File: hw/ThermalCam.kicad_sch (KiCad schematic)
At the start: 48 parts, among them J1 Conn_02x20_Counter_Clockwise, J2 Conn_01x04, J3 Conn_01x06, U1 GW1NR-9_QN882, X1 ASE-25MHz

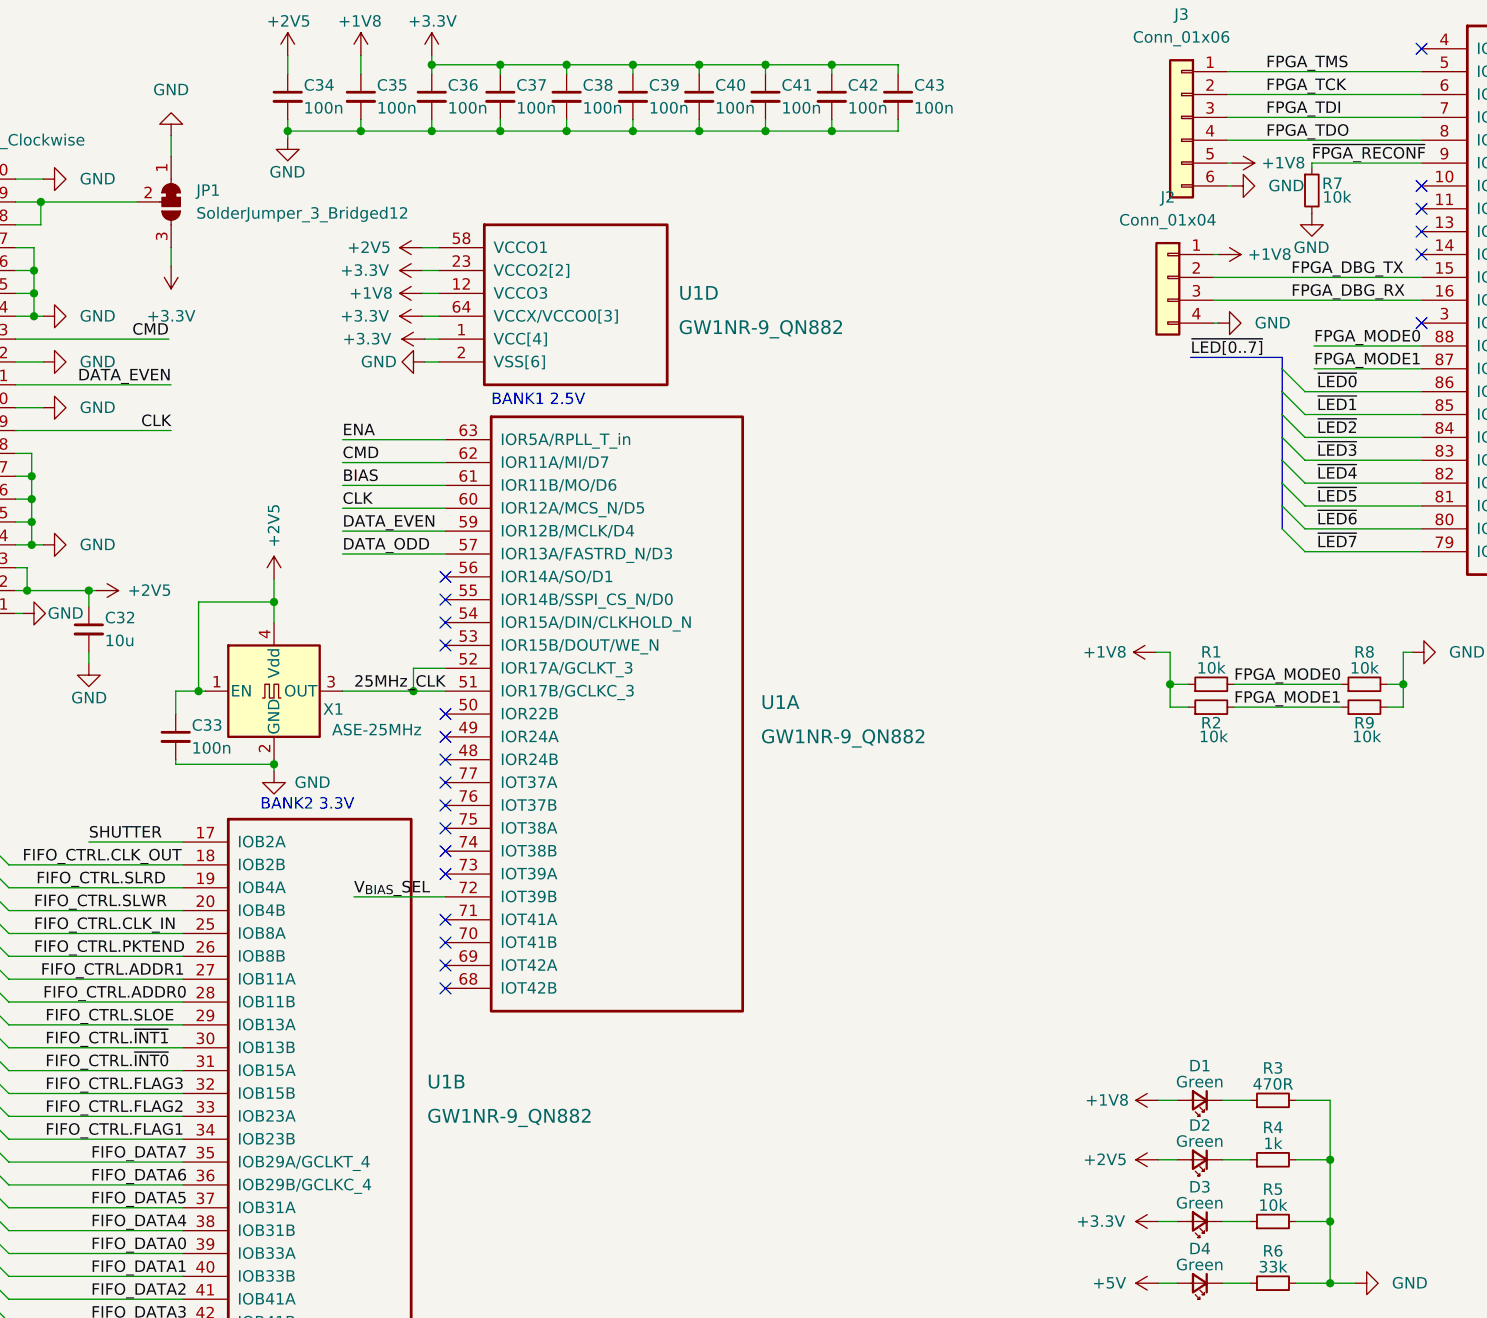
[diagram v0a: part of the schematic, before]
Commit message: schematic fixes and adding sw section
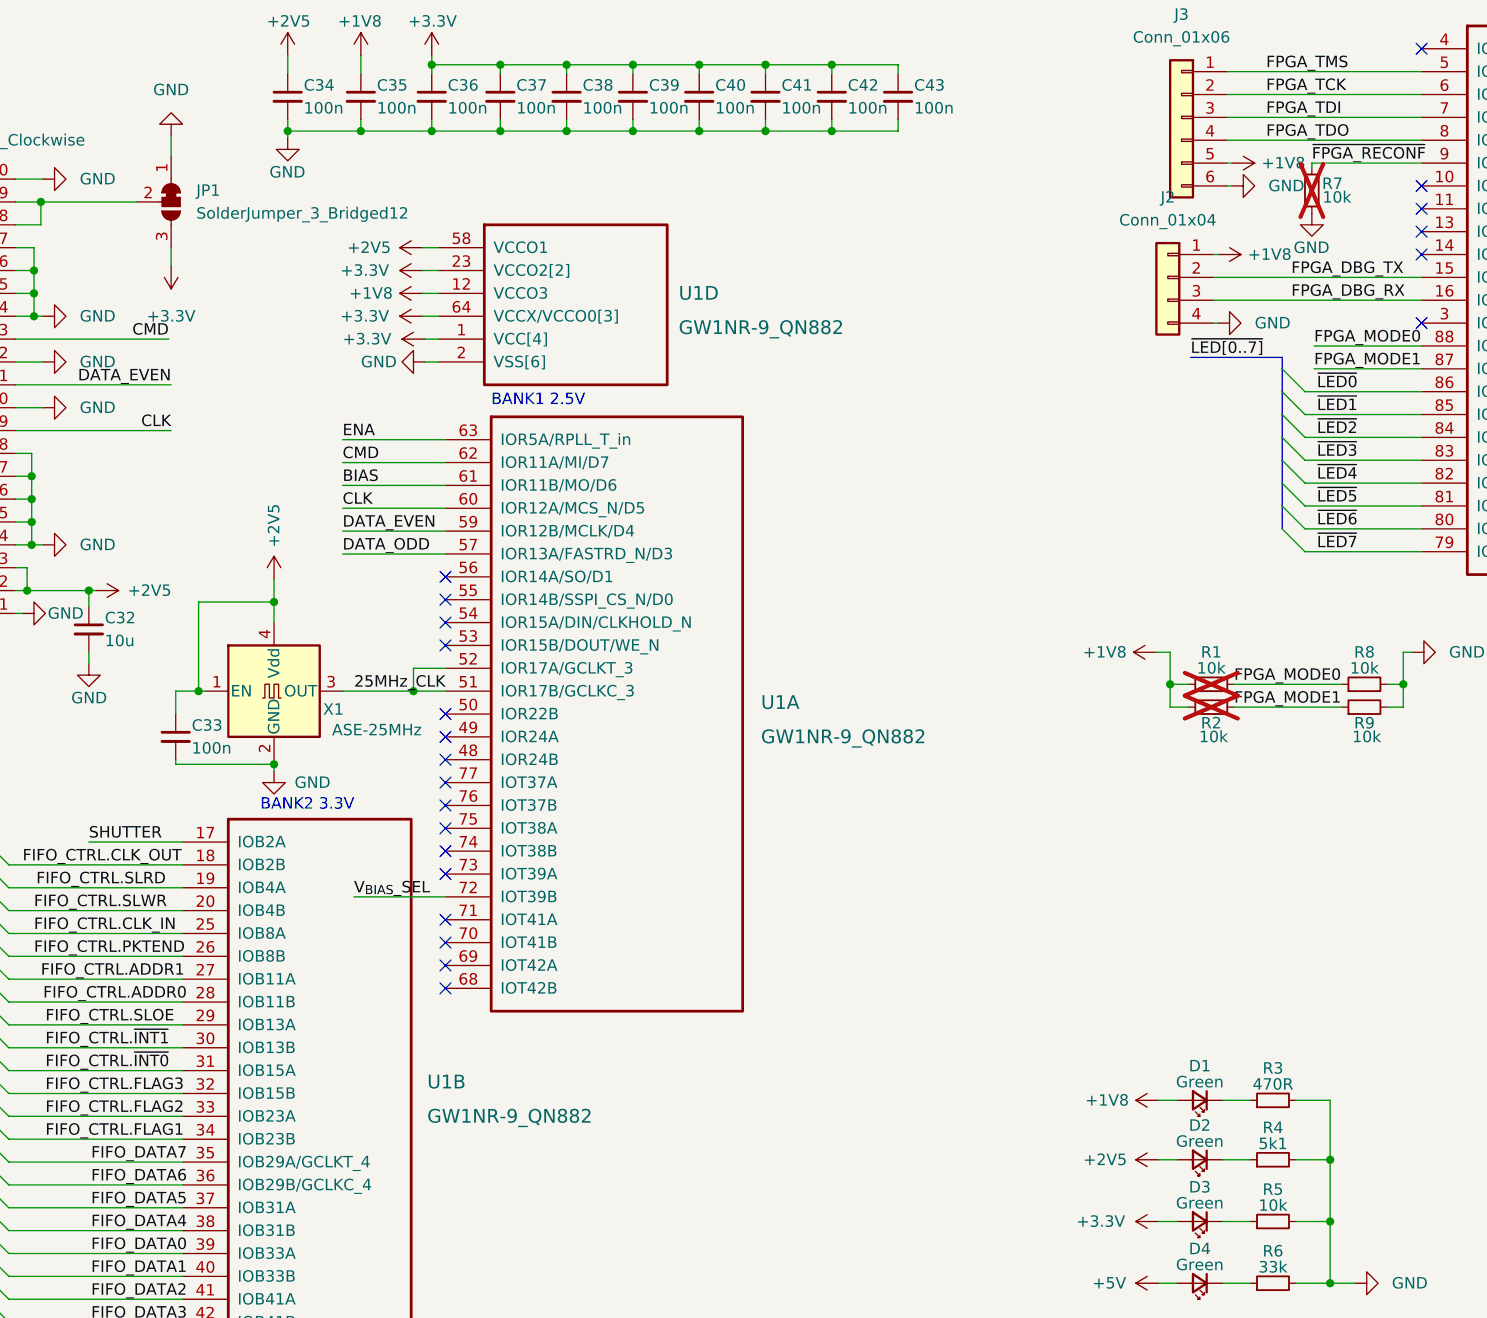
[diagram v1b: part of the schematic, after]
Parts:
- R1, R2, R7: now not fitted
- R4: value 1k -> 5k1
